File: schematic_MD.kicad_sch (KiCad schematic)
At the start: 32 parts, among them J1 XT60, J10 Gate_PWR_Jump, J13 EXPWR_GND, J2 XT60, J3 XT60, J4 CAN_Bus, J5 Rotaly_encoder_1, J6 Rotaly_encoder_2, J7 Z_jumper, J8 Z_jumper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

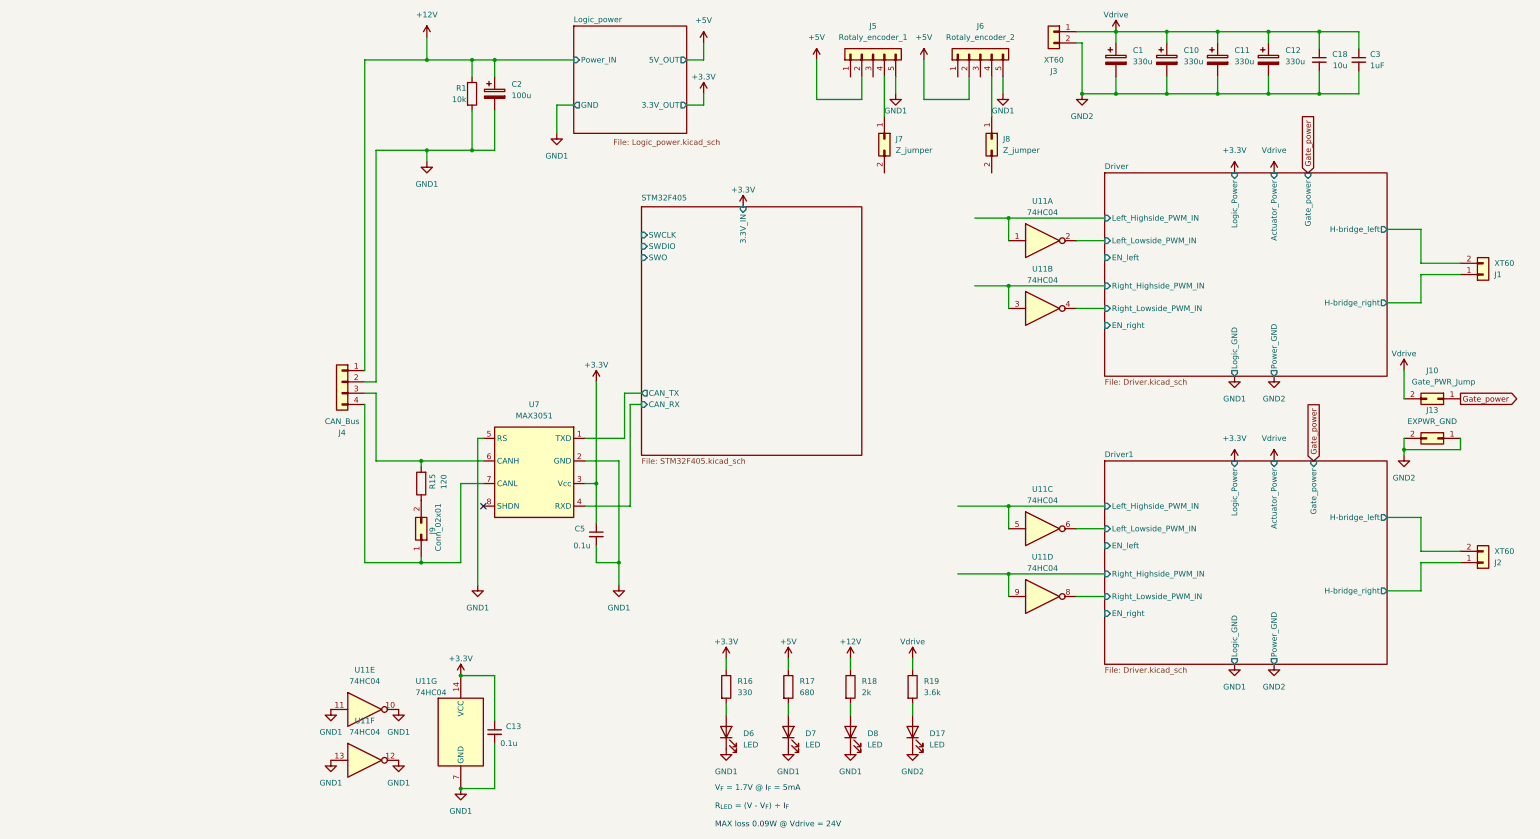
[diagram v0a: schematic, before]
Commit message: add logic parts
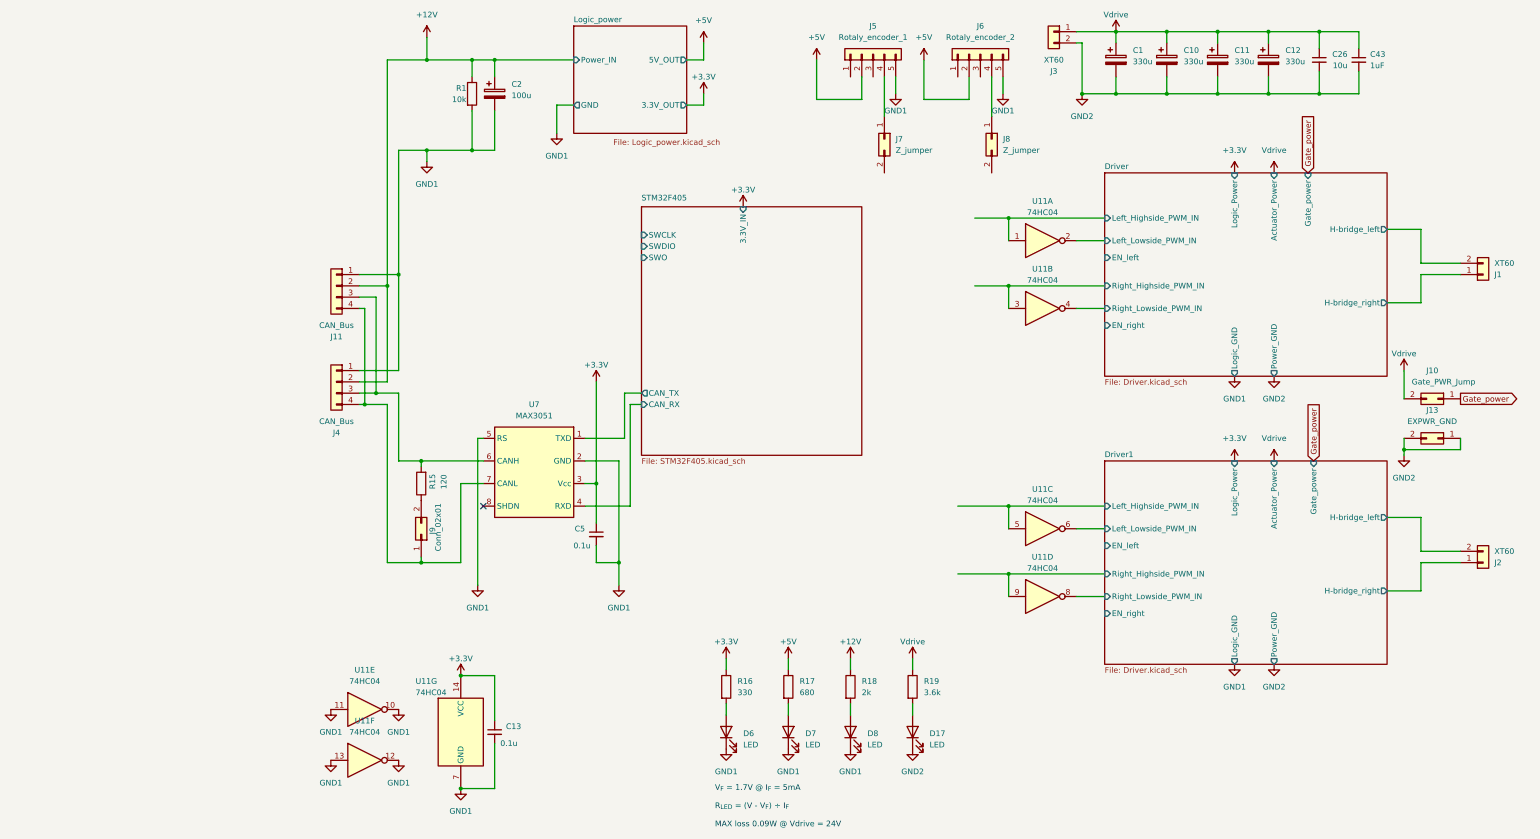
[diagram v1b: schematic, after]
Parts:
- added J11: CAN_Bus, Connector_JST:JST_XA_B04B-XASK-1_1x04_P2.50mm_Vertical, symbol Connector_Generic:Conn_01x04
- C13, C5: footprint Capacitor_SMD:C_01005_0402Metric_Pad0.57x0.30mm_HandSolder -> Capacitor_SMD:C_0402_1005Metric_Pad0.74x0.62mm_HandSolder
- renumbered C18 to C26, C3 to C43
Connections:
- net +12V: now also J4.2 (Pin_2), J11.2 (Pin_2); no longer J4.1 (Pin_1)
- net GND1: now also J4.1 (Pin_1), J11.1 (Pin_1); no longer J4.2 (Pin_2)
- net at J4.3 (Pin_3), R15.2, U7.6 (CANH): now also J11.3 (Pin_3)
- net at J4.4 (Pin_4), J9.1 (Pin_1), U7.7 (CANL): now also J11.4 (Pin_4)
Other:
- moved on the sheet: J4
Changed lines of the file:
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@@
   (junction (at 38.1 114.3) (diameter 0) (color 0 0 0 0)
   )
+  (junction (at 25.4 101.6) (diameter 0) (color 0 0 0 0)
+  )
   (junction (at 54.61 24.13) (diameter 0) (color 0 0 0 0)
   )
@@
   (junction (at 194.31 31.75) (diameter 0) (color 0 0 0 0)
   )
+  (junction (at 30.48 74.93) (diameter 0) (color 0 0 0 0)
+  )
+  (junction (at 33.02 72.39) (diameter 0) (color 0 0 0 0)
+  )
   (junction (at 259.08 111.76) (diameter 0) (color 0 0 0 0)
+  )
+  (junction (at 27.94 99.06) (diameter 0) (color 0 0 0 0)
   )
   (junction (at 217.17 31.75) (diameter 0) (color 0 0 0 0)
@@
     (stroke (width 0) (type default))
   )
+  (wire (pts (xy 24.13 72.39) (xy 33.02 72.39))
+    (stroke (width 0) (type default))
+  )
   (wire (pts (xy 240.03 31.75) (xy 228.6 31.75))
     (stroke (width 0) (type default))
@@
     (stroke (width 0) (type default))
   )
+  (wire (pts (xy 24.13 77.47) (xy 27.94 77.47))
+    (stroke (width 0) (type default))
+  )
   (wire (pts (xy 158.75 139.7) (xy 170.18 139.7))
     (stroke (width 0) (type default))
@@
     (stroke (width 0) (type default))
   )
-  (wire (pts (xy 25.4 101.6) (xy 25.4 137.16))
+  (wire (pts (xy 30.48 101.6) (xy 30.48 137.16))
     (stroke (width 0) (type default))
   )
@@
     (stroke (width 0) (type default))
   )
+  (wire (pts (xy 24.13 99.06) (xy 27.94 99.06))
+    (stroke (width 0) (type default))
+  )
   (wire (pts (xy 38.1 135.89) (xy 38.1 137.16))
     (stroke (width 0) (type default))
@@
     (stroke (width 0) (type default))
   )
-  (wire (pts (xy 27.94 96.52) (xy 25.4 96.52))
-    (stroke (width 0) (type default))
-  )
   (wire (pts (xy 271.78 109.22) (xy 271.78 111.76))
     (stroke (width 0) (type default))
@@
     (stroke (width 0) (type default))
   )
-  (wire (pts (xy 27.94 44.45) (xy 27.94 96.52))
+  (wire (pts (xy 33.02 44.45) (xy 33.02 72.39))
     (stroke (width 0) (type default))
   )
@@
     (stroke (width 0) (type default))
   )
+  (wire (pts (xy 24.13 93.98) (xy 33.02 93.98))
+    (stroke (width 0) (type default))
+  )
   (wire (pts (xy 185.42 129.54) (xy 191.77 129.54))
     (stroke (width 0) (type default))
@@
     (stroke (width 0) (type default))
   )
-  (wire (pts (xy 39.37 24.13) (xy 25.4 24.13))
+  (wire (pts (xy 39.37 24.13) (xy 30.48 24.13))
     (stroke (width 0) (type default))
   )
@@
     (stroke (width 0) (type default))
   )
+  (wire (pts (xy 30.48 101.6) (xy 25.4 101.6))
+    (stroke (width 0) (type default))
+  )
   (wire (pts (xy 54.61 27.94) (xy 54.61 24.13))
     (stroke (width 0) (type default))
@@
     (stroke (width 0) (type default))
   )
-  (wire (pts (xy 39.37 44.45) (xy 27.94 44.45))
-    (stroke (width 0) (type default))
-  )
-  (wire (pts (xy 25.4 137.16) (xy 38.1 137.16))
+  (wire (pts (xy 39.37 44.45) (xy 33.02 44.45))
+    (stroke (width 0) (type default))
+  )
+  (wire (pts (xy 30.48 137.16) (xy 38.1 137.16))
     (stroke (width 0) (type default))
   )
@@
     (stroke (width 0) (type default))
   )
-  (wire (pts (xy 27.94 99.06) (xy 25.4 99.06))
+  (wire (pts (xy 33.02 99.06) (xy 27.94 99.06))
     (stroke (width 0) (type default))
   )
@@
     (stroke (width 0) (type default))
   )
+  (wire (pts (xy 24.13 80.01) (xy 25.4 80.01))
+    (stroke (width 0) (type default))
+  )
   (wire (pts (xy 217.17 31.75) (xy 228.6 31.75))
     (stroke (width 0) (type default))
@@
     (stroke (width 0) (type default))
   )
-  (wire (pts (xy 25.4 24.13) (xy 25.4 93.98))
-    (stroke (width 0) (type default))
-  )
   (wire (pts (xy 39.37 19.05) (xy 39.37 24.13))
     (stroke (width 0) (type default))
@@
     (stroke (width 0) (type default))
   )
-  (wire (pts (xy 27.94 114.3) (xy 38.1 114.3))
+  (wire (pts (xy 33.02 114.3) (xy 38.1 114.3))
     (stroke (width 0) (type default))
   )
@@
     (stroke (width 0) (type default))
   )
+  (wire (pts (xy 30.48 74.93) (xy 30.48 96.52))
+    (stroke (width 0) (type default))
+  )
+  (wire (pts (xy 24.13 96.52) (xy 30.48 96.52))
+    (stroke (width 0) (type default))
+  )
   (wire (pts (xy 240.03 21.59) (xy 240.03 17.78))
     (stroke (width 0) (type default))
@@
     (stroke (width 0) (type default))
   )
+  (wire (pts (xy 30.48 24.13) (xy 30.48 74.93))
+    (stroke (width 0) (type default))
+  )
   (wire (pts (xy 168.91 27.94) (xy 168.91 31.75))
     (stroke (width 0) (type default))
@@
     (stroke (width 0) (type default))
   )
+  (wire (pts (xy 24.13 74.93) (xy 30.48 74.93))
+    (stroke (width 0) (type default))
+  )
   (wire (pts (xy 262.89 72.39) (xy 271.78 72.39))
     (stroke (width 0) (type default))
   )
-  (wire (pts (xy 27.94 114.3) (xy 27.94 99.06))
+  (wire (pts (xy 33.02 114.3) (xy 33.02 99.06))
     (stroke (width 0) (type default))
   )
@@
     (stroke (width 0) (type default))
   )
+  (wire (pts (xy 25.4 101.6) (xy 24.13 101.6))
+    (stroke (width 0) (type default))
+  )
+  (wire (pts (xy 33.02 72.39) (xy 33.02 93.98))
+    (stroke (width 0) (type default))
+  )
   (wire (pts (xy 137.16 27.94) (xy 137.16 33.02))
     (stroke (width 0) (type default))
   )
+  (wire (pts (xy 25.4 80.01) (xy 25.4 101.6))
+    (stroke (width 0) (type default))
+  )
   (wire (pts (xy 54.61 177.8) (xy 54.61 187.96))
     (stroke (width 0) (type default))
@@
   )
   (wire (pts (xy 194.31 31.75) (xy 194.31 27.94))
+    (stroke (width 0) (type default))
+  )
+  (wire (pts (xy 27.94 77.47) (xy 27.94 99.06))
     (stroke (width 0) (type default))
   )
@@
     )
   )
+  (symbol (lib_id "Connector_Generic:Conn_01x04") (at 19.05 74.93 0) (mirror y) (unit 1)
+    (in_bom yes) (on_board yes) (dnp no)
+    (property "Reference" "J11" (at 19.05 86.36 0)
+      (effects (font (size 1.27 1.27)))
+    )
+    (property "Value" "CAN_Bus" (at 19.05 83.82 0)
+      (effects (font (size 1.27 1.27)))
+    )
+    (property "Footprint" "Connector_JST:JST_XA_B04B-XASK-1_1x04_P2.50mm_Vertical" (at 19.05 74.93 0)
+      (effects (font (size 1.27 1.27)) hide)
+    )
+    (property "Datasheet" "~" (at 19.05 74.93 0)
+      (effects (font (size 1.27 1.27)) hide)
+    )
+    (pin "1")
+    (pin "2")
+    (pin "3")
+    (pin "4")
+    (instances
+      (project "schematic_MD"
+        (path "/3152684b-d11f-4a9a-8e6c-09965044adbd"
+          (reference "J11") (unit 1)
+        )
+      )
+    )
+  )
   (symbol (lib_id "Device:C_Polarized") (at 217.17 24.13 0) (unit 1)
     (in_bom yes) (on_board yes) (dnp no) (fields_autoplaced)
@@
       (effects (font (size 1.27 1.27)) (justify right))
     )
-    (property "Footprint" "Capacitor_SMD:C_01005_0402Metric_Pad0.57x0.30mm_HandSolder" (at 54.61 175.26 0)
+    (property "Footprint" "Capacitor_SMD:C_0402_1005Metric_Pad0.74x0.62mm_HandSolder" (at 54.61 175.26 0)
       (effects (font (size 1.27 1.27)) hide)
     )
@@
   (symbol (lib_id "Device:C_Small") (at 240.03 24.13 0) (unit 1)
     (in_bom yes) (on_board yes) (dnp no)
-    (property "Reference" "C18" (at 246.38 22.86 0)
+    (property "Reference" "C26" (at 246.38 22.86 0)
       (effects (font (size 1.27 1.27)) (justify right))
     )
@@
     (instances
       (project "schematic_MD"
-        (path "/3152684b-d11f-4a9a-8e6c-09965044adbd/c42baef9-5835-4e28-8d2a-6c2cc5412fde"
-          (reference "C18") (unit 1)
-        )
-        (path "/3152684b-d11f-4a9a-8e6c-09965044adbd/d6563a9b-6b27-49bf-ae38-0382291b0c3e"
-          (reference "C23") (unit 1)
-        )
         (path "/3152684b-d11f-4a9a-8e6c-09965044adbd"
           (reference "C26") (unit 1)
@@
     )
   )
-  (symbol (lib_id "Connector_Generic:Conn_01x04") (at 20.32 96.52 0) (mirror y) (unit 1)
-    (in_bom yes) (on_board yes) (dnp no)
-    (property "Reference" "J4" (at 20.32 107.95 0)
-      (effects (font (size 1.27 1.27)))
-    )
-    (property "Value" "CAN_Bus" (at 20.32 105.41 0)
-      (effects (font (size 1.27 1.27)))
-    )
-    (property "Footprint" "Connector_JST:JST_XA_B04B-XASK-1_1x04_P2.50mm_Vertical" (at 20.32 96.52 0)
-      (effects (font (size 1.27 1.27)) hide)
-    )
-    (property "Datasheet" "~" (at 20.32 96.52 0)
+  (symbol (lib_id "Connector_Generic:Conn_01x04") (at 19.05 96.52 0) (mirror y) (unit 1)
+    (in_bom yes) (on_board yes) (dnp no)
+    (property "Reference" "J4" (at 19.05 107.95 0)
+      (effects (font (size 1.27 1.27)))
+    )
+    (property "Value" "CAN_Bus" (at 19.05 105.41 0)
+      (effects (font (size 1.27 1.27)))
+    )
+    (property "Footprint" "Connector_JST:JST_XA_B04B-XASK-1_1x04_P2.50mm_Vertical" (at 19.05 96.52 0)
+      (effects (font (size 1.27 1.27)) hide)
+    )
+    (property "Datasheet" "~" (at 19.05 96.52 0)
       (effects (font (size 1.27 1.27)) hide)
     )
@@
       (effects (font (size 1.27 1.27)) (justify right))
     )
-    (property "Footprint" "Capacitor_SMD:C_01005_0402Metric_Pad0.57x0.30mm_HandSolder" (at 77.47 130.81 0)
+    (property "Footprint" "Capacitor_SMD:C_0402_1005Metric_Pad0.74x0.62mm_HandSolder" (at 77.47 130.81 0)
       (effects (font (size 1.27 1.27)) hide)
     )
@@
   (symbol (lib_id "Device:C_Small") (at 248.92 24.13 0) (mirror y) (unit 1)
     (in_bom yes) (on_board yes) (dnp no)
-    (property "Reference" "C3" (at 251.46 22.8663 0)
+    (property "Reference" "C43" (at 251.46 22.8663 0)
       (effects (font (size 1.27 1.27)) (justify right))
     )
@@
     (instances
       (project "schematic_MD"
-        (path "/3152684b-d11f-4a9a-8e6c-09965044adbd/2d267caf-42fc-44ea-97db-65c2b77a1587"
-          (reference "C3") (unit 1)
-        )
         (path "/3152684b-d11f-4a9a-8e6c-09965044adbd"
           (reference "C43") (unit 1)

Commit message: fix logic
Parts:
- removed J7, J8: Z_jumper, Connector_PinHeader_2.54mm:PinHeader_1x02_P2.54mm_Vertical, symbol Connector_Generic:Conn_02x01
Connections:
- net GND1: now also J5.1 (Pin_1), J6.1 (Pin_1); no longer J5.5 (Pin_5), J6.5 (Pin_5)
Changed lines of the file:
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@@
-    (stroke (width 0) (type default))
-  )
-  (wire (pts (xy 142.24 27.94) (xy 142.24 36.83))
     (stroke (width 0) (type default))
   )
@@
     (stroke (width 0) (type default))
   )
-  (wire (pts (xy 166.37 27.94) (xy 166.37 36.83))
-    (stroke (width 0) (type default))
-  )
   (wire (pts (xy 186.69 31.75) (xy 194.31 31.75))
     (stroke (width 0) (type default))
@@
     (stroke (width 0) (type default))
   )
-  (wire (pts (xy 144.78 27.94) (xy 144.78 31.75))
-    (stroke (width 0) (type default))
-  )
   (wire (pts (xy 49.53 35.56) (xy 49.53 44.45))
     (stroke (width 0) (type default))
@@
     (stroke (width 0) (type default))
   )
+  (wire (pts (xy 158.75 27.94) (xy 158.75 36.83))
+    (stroke (width 0) (type default))
+  )
   (wire (pts (xy 255.27 62.23) (xy 262.89 62.23))
     (stroke (width 0) (type default))
@@
     (stroke (width 0) (type default))
   )
+  (wire (pts (xy 134.62 27.94) (xy 134.62 36.83))
+    (stroke (width 0) (type default))
+  )
   (wire (pts (xy 33.02 44.45) (xy 33.02 72.39))
     (stroke (width 0) (type default))
@@
   )
   (wire (pts (xy 30.48 24.13) (xy 30.48 74.93))
-    (stroke (width 0) (type default))
-  )
-  (wire (pts (xy 168.91 27.94) (xy 168.91 31.75))
     (stroke (width 0) (type default))
   )
@@
     )
   )
-  (symbol (lib_id "power:GND1") (at 144.78 31.75 0) (unit 1)
-    (in_bom yes) (on_board yes) (dnp no)
-    (property "Reference" "#PWR07" (at 144.78 38.1 0)
-      (effects (font (size 1.27 1.27)) hide)
-    )
-    (property "Value" "GND1" (at 144.78 35.56 0)
-      (effects (font (size 1.27 1.27)))
-    )
-    (property "Footprint" "" (at 144.78 31.75 0)
-      (effects (font (size 1.27 1.27)) hide)
-    )
-    (property "Datasheet" "" (at 144.78 31.75 0)
-      (effects (font (size 1.27 1.27)) hide)
-    )
-    (pin "1")
-    (instances
-      (project "schematic_MD"
-        (path "/3152684b-d11f-4a9a-8e6c-09965044adbd"
-          (reference "#PWR07") (unit 1)
-        )
-      )
-    )
-  )
   (symbol (lib_id "power:GND1") (at 82.55 142.24 0) (unit 1)
     (in_bom yes) (on_board yes) (dnp no) (fields_autoplaced)
@@
     )
   )
+  (symbol (lib_id "power:GND1") (at 158.75 36.83 0) (unit 1)
+    (in_bom yes) (on_board yes) (dnp no)
+    (property "Reference" "#PWR09" (at 158.75 43.18 0)
+      (effects (font (size 1.27 1.27)) hide)
+    )
+    (property "Value" "GND1" (at 158.75 40.64 0)
+      (effects (font (size 1.27 1.27)))
+    )
+    (property "Footprint" "" (at 158.75 36.83 0)
+      (effects (font (size 1.27 1.27)) hide)
+    )
+    (property "Datasheet" "" (at 158.75 36.83 0)
+      (effects (font (size 1.27 1.27)) hide)
+    )
+    (pin "1")
+    (instances
+      (project "schematic_MD"
+        (path "/3152684b-d11f-4a9a-8e6c-09965044adbd"
+          (reference "#PWR09") (unit 1)
+        )
+      )
+    )
+  )
   (symbol (lib_id "Connector_Generic:Conn_01x02") (at 276.86 72.39 0) (mirror x) (unit 1)
     (in_bom yes) (on_board yes) (dnp no)
@@
         (path "/3152684b-d11f-4a9a-8e6c-09965044adbd"
           (reference "R1") (unit 1)
+        )
+      )
+    )
+  )
+  (symbol (lib_id "power:GND1") (at 134.62 36.83 0) (unit 1)
+    (in_bom yes) (on_board yes) (dnp no)
+    (property "Reference" "#PWR07" (at 134.62 43.18 0)
+      (effects (font (size 1.27 1.27)) hide)
+    )
+    (property "Value" "GND1" (at 134.62 40.64 0)
+      (effects (font (size 1.27 1.27)))
+    )
+    (property "Footprint" "" (at 134.62 36.83 0)
+      (effects (font (size 1.27 1.27)) hide)
+    )
+    (property "Datasheet" "" (at 134.62 36.83 0)
+      (effects (font (size 1.27 1.27)) hide)
+    )
+    (pin "1")
+    (instances
+      (project "schematic_MD"
+        (path "/3152684b-d11f-4a9a-8e6c-09965044adbd"
+          (reference "#PWR07") (unit 1)
         )
       )
@@
     )
   )
-  (symbol (lib_id "power:GND1") (at 168.91 31.75 0) (unit 1)
-    (in_bom yes) (on_board yes) (dnp no)
-    (property "Reference" "#PWR09" (at 168.91 38.1 0)
-      (effects (font (size 1.27 1.27)) hide)
-    )
-    (property "Value" "GND1" (at 168.91 35.56 0)
-      (effects (font (size 1.27 1.27)))
-    )
-    (property "Footprint" "" (at 168.91 31.75 0)
-      (effects (font (size 1.27 1.27)) hide)
-    )
-    (property "Datasheet" "" (at 168.91 31.75 0)
-      (effects (font (size 1.27 1.27)) hide)
-    )
-    (pin "1")
-    (instances
-      (project "schematic_MD"
-        (path "/3152684b-d11f-4a9a-8e6c-09965044adbd"
-          (reference "#PWR09") (unit 1)
-        )
-      )
-    )
-  )
   (symbol (lib_id "power:Vdrive") (at 259.08 93.98 0) (mirror y) (unit 1)
     (in_bom yes) (on_board yes) (dnp no)
@@
     )
   )
-  (symbol (lib_id "Connector_Generic:Conn_02x01") (at 166.37 41.91 270) (unit 1)
-    (in_bom yes) (on_board yes) (dnp no) (fields_autoplaced)
-    (property "Reference" "J8" (at 168.91 41.91 90)
-      (effects (font (size 1.27 1.27)) (justify left))
-    )
-    (property "Value" "Z_jumper" (at 168.91 44.45 90)
-      (effects (font (size 1.27 1.27)) (justify left))
-    )
-    (property "Footprint" "Connector_PinHeader_2.54mm:PinHeader_1x02_P2.54mm_Vertical" (at 166.37 41.91 0)
-      (effects (font (size 1.27 1.27)) hide)
-    )
-    (property "Datasheet" "~" (at 166.37 41.91 0)
-      (effects (font (size 1.27 1.27)) hide)
-    )
-    (pin "2")
-    (pin "1")
-    (instances
-      (project "schematic_MD"
-        (path "/3152684b-d11f-4a9a-8e6c-09965044adbd"
-          (reference "J8") (unit 1)
-        )
-      )
-    )
-  )
   (symbol (lib_id "74xx:74HC04") (at 177.8 129.54 0) (unit 3)
     (in_bom yes) (on_board yes) (dnp no) (fields_autoplaced)
@@
         )
       )
-    )
-  )
-  (symbol (lib_id "Connector_Generic:Conn_02x01") (at 142.24 41.91 270) (unit 1)
-    (in_bom yes) (on_board yes) (dnp no) (fields_autoplaced)
-    (property "Reference" "J7" (at 144.78 41.91 90)
-      (effects (font (size 1.27 1.27)) (justify left))
-    )
-    (property "Value" "Z_jumper" (at 144.78 44.45 90)
-      (effects (font (size 1.27 1.27)) (justify left))
-    )
-    (property "Footprint" "Connector_PinHeader_2.54mm:PinHeader_1x02_P2.54mm_Vertical" (at 142.24 41.91 0)
-      (effects (font (size 1.27 1.27)) hide)
-    )
-    (property "Datasheet" "~" (at 142.24 41.91 0)
-      (effects (font (size 1.27 1.27)) hide)
-    )
-    (pin "2")
-    (pin "1")
-    (instances
-      (project "schematic_MD"
-        (path "/3152684b-d11f-4a9a-8e6c-09965044adbd"
-          (reference "J7") (unit 1)
-        )
-      )
